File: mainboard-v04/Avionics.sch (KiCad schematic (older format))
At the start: 36 parts, among them J10 Conn_01x05, J8 Conn_01x09, J9 Conn_01x05, SW1 KMR231NG LFS, U1 MAX706RS-T, U2 ATSAMD51J20A-AU, U3 BMX160, Y1 32.768kHz

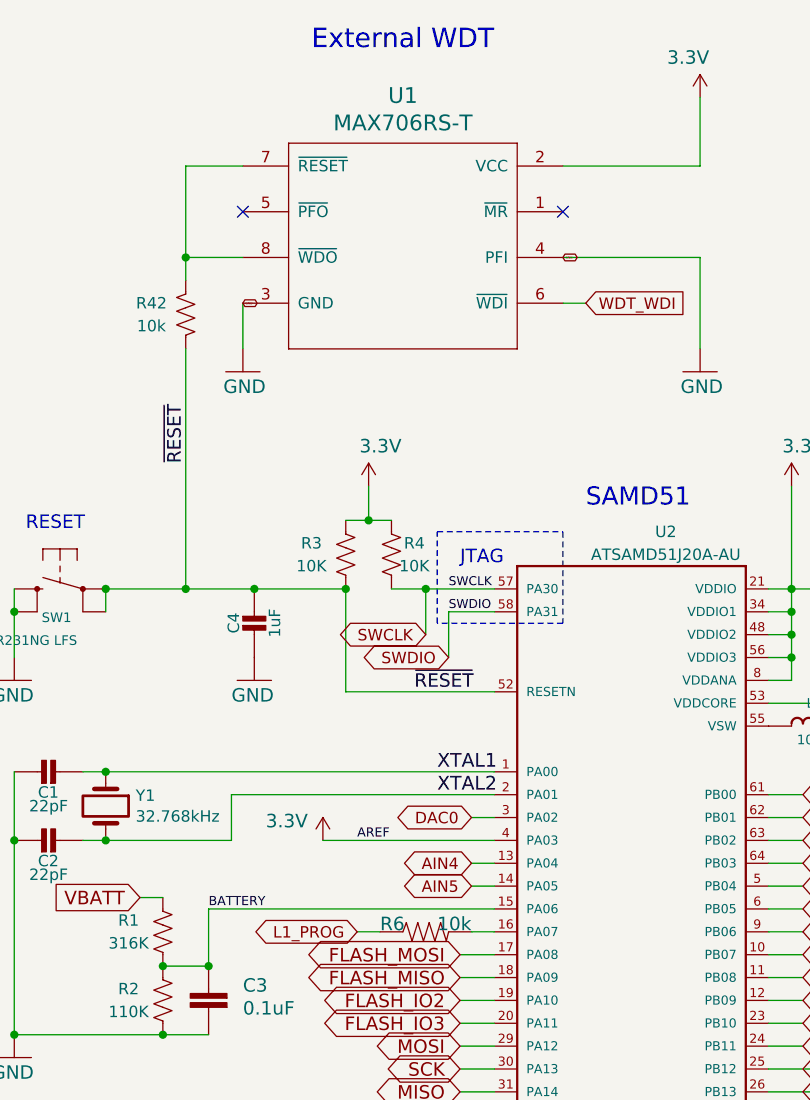
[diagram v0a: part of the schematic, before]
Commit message: adding mainbaordv04 layout and BOM
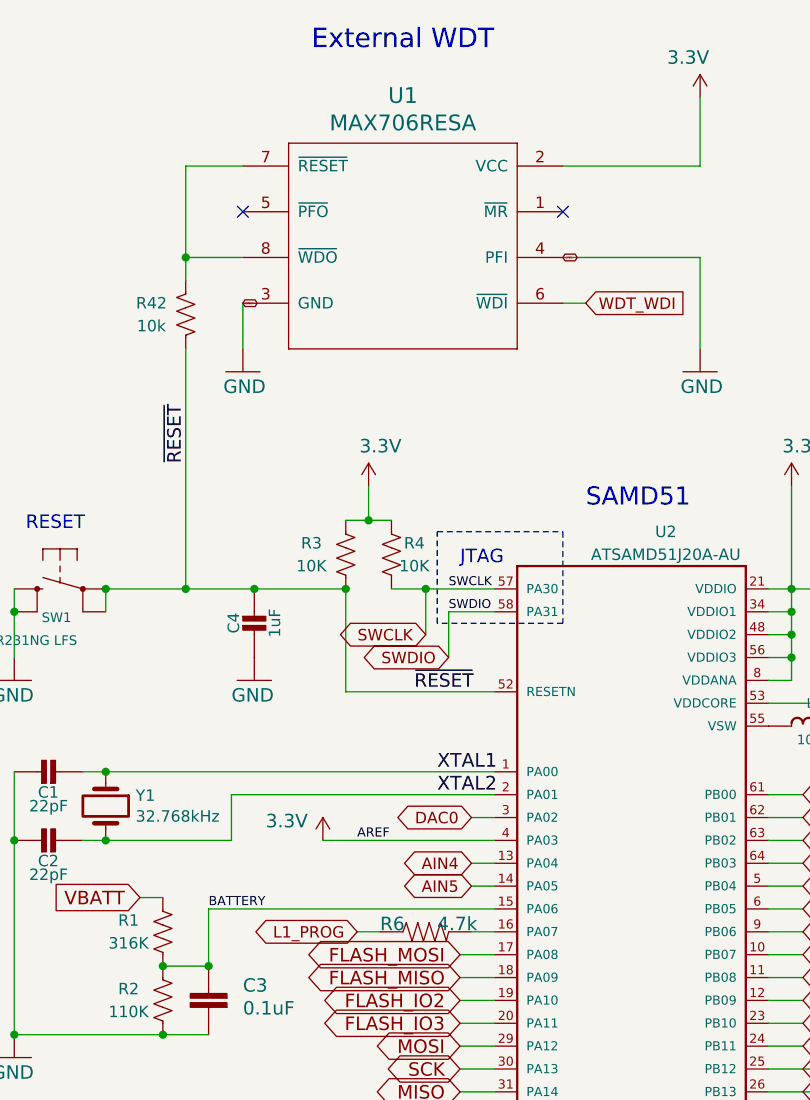
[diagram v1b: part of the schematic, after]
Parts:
- D1: Flight (none) -> WS2812B; Proto (none) -> WS2812B
- L1: footprint Inductor_SMD:L_0806_2016Metric -> Inductor_SMD:L_0805_2012Metric_Pad1.15x1.40mm_HandSolder
- R6: value 10k -> 4.7k
- U1: value MAX706RS-T -> MAX706RESA; Flight (none) -> MAX706RESA; Proto (none) -> MAX706RESA
- U2: Field8 Unavailable -> (none); Flight (none) -> ATSAMD51J20A-AU; Proto (none) -> ATSAMD51J20A-AU
- U3: Flight (none) -> BMX160; Height 1 -> (none); Manufacturer_Name Bosch -> (none); Manufacturer_Part_Number BMX160 -> (none); Mouser Part Number 262-BMX160 -> (none); Proto (none) -> BMX160
- Y1: Flight (none) -> ABS07-32.768KHZ-T; Proto (none) -> ABS07-32.768KHZ-T
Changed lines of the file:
@@
 EESchema Schematic File Version 4
-LIBS:mainboard-cache
 EELAYER 30 0
 EELAYER END
@@
 Sheet 6 6
 Title "PyCubed Mainboard"
-Date "2019-11-27"
+Date "2020-01-08"
 Rev "v04"
-Comp "Stanford University"
+Comp ""
 Comment1 "Zac Manchester"
 Comment2 "Max Holliday"
@@
 AR Path="/5CEC5A72/B13F4994" Ref="R6"  Part="1"
 F 0 "R6" H 4200 4650 59  0000 L BNN
-F 1 "10k" H 4450 4650 59  0000 L BNN
+F 1 "4.7k" H 4450 4650 59  0000 L BNN
 F 2 "Resistor_SMD:R_0603_1608Metric" H 4400 4650 50  0001 C CNN
 F 3 "" H 4400 4650 50  0001 C CNN
@@
 F 0 "L1" H 6100 3850 42  0000 C CNN
 F 1 "10uH" H 6100 3690 42  0000 C CNN
-F 2 "Inductor_SMD:L_0806_2016Metric" H 6100 3750 50  0001 C CNN
+F 2 "Inductor_SMD:L_0805_2012Metric_Pad1.15x1.40mm_HandSolder" H 6100 3750 50  0001 C CNN
 F 3 "https://product.tdk.com/info/en/catalog/datasheets/inductor_commercial_power_vls201610hbx-1_en.pdf" H 6100 3750 50  0001 C CNN
 	1    6100 3750
@@
 F 2 "Crystal:Crystal_SMD_3215-2Pin_3.2x1.5mm" H 3000 4100 50  0001 C CNN
 F 3 "~" H 3000 4100 50  0001 C CNN
+F 4 "ABS07-32.768KHZ-T" H 3000 4100 50  0001 C CNN "Flight"
+F 5 "ABS07-32.768KHZ-T" H 3000 4100 50  0001 C CNN "Proto"
 	1    3000 4100
 	0    1    1    0
@@
 P 5100 1400
 F 0 "U1" H 5900 1808 69  0000 C CNN
-F 1 "MAX706RS-T" H 5900 1688 69  0000 C CNN
+F 1 "MAX706RESA" H 5900 1688 69  0000 C CNN
 F 2 "Package_SO:SO-8_3.9x4.9mm_P1.27mm" H 5100 1400 50  0001 C CNN
 F 3 "" H 5100 1400 50  0001 C CNN
+F 4 "MAX706RESA" H 5100 1400 50  0001 C CNN "Flight"
+F 5 "MAX706RESA" H 5100 1400 50  0001 C CNN "Proto"
 	1    5100 1400
 	-1   0    0    -1
@@
 F 6 "None" H 5300 4950 50  0001 L BNN "Field6"
 F 7 "ATSAMD51J20A-AU" H 5300 4950 50  0001 L BNN "Field7"
-F 8 "Unavailable" H 5300 4950 50  0001 L BNN "Field8"
+F 8 "" H 5300 4950 50  0001 L BNN "Field8"
+F 9 "ATSAMD51J20A-AU" H 5300 4950 50  0001 C CNN "Flight"
+F 10 "ATSAMD51J20A-AU" H 5300 4950 50  0001 C CNN "Proto"
 	1    5300 4950
 	1    0    0    -1
@@
 F 2 "LED_SMD:LED_WS2812B_PLCC4_5.0x5.0mm_P3.2mm" H 3150 5750 50  0001 L TNN
 F 3 "https://cdn-shop.adafruit.com/datasheets/WS2812B.pdf" H 3200 5675 50  0001 L TNN
+F 4 "WS2812B" H 3100 6050 50  0001 C CNN "Flight"
+F 5 "WS2812B" H 3100 6050 50  0001 C CNN "Proto"
 	1    3100 6050
 	-1   0    0    -1
@@
 F 3 "https://ae-bst.resource.bosch.com/media/_tech/media/datasheets/BST-BMX160-DS000.pdf" H 10250 4850 50  0001 L CNN
 F 4 "IMUs - Inertial Measurement Units 9-axis (9DOF) Absolute Orientation MEMS Sensor" H 10250 4750 50  0001 L CNN "Description"
-F 5 "1" H 10250 4650 50  0001 L CNN "Height"
-F 6 "Bosch" H 10250 4550 50  0001 L CNN "Manufacturer_Name"
-F 7 "BMX160" H 10250 4450 50  0001 L CNN "Manufacturer_Part_Number"
-F 8 "262-BMX160" H 10250 4350 50  0001 L CNN "Mouser Part Number"
+F 5 "" H 10250 4650 50  0001 L CNN "Height"
+F 6 "" H 10250 4550 50  0001 L CNN "Manufacturer_Name"
+F 7 "" H 10250 4450 50  0001 L CNN "Manufacturer_Part_Number"
+F 8 "" H 10250 4350 50  0001 L CNN "Mouser Part Number"
+F 9 "BMX160" H 9200 4850 50  0001 C CNN "Flight"
+F 10 "BMX160" H 9200 4850 50  0001 C CNN "Proto"
 	1    9200 4850
 	-1   0    0    -1

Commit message: cleaned up v04
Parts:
- added C5: 0.1uF, Capacitor_SMD:C_0603_1608Metric, symbol mainboard:0.1UF-25V(+80_-20%)(0603)
- added R41: 10k, Resistor_SMD:R_0603_1608Metric, symbol mainboard:R-US_R0603
- J10, J8, J9, R42: DNI (none) -> DNI
- U2: value ATSAMD51J20A-AU -> 120MHZ 512KB Flash 64 TQFP; Field4 120MHZ 1024KB Flash 64 TQFP PKG inTray 85CTemp, 64 TQFP 10x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 -> 120MHZ 512KB Flash 64 TQFP PKG inTray 85CTemp, 64 TQFP 10x1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; Field6 None -> (none); Field7 ATSAMD51J20A-AU -> (none); Flight ATSAMD51J20A-AU -> ATSAMD51J19A-AU; Proto ATSAMD51J20A-AU -> ATSAMD51J19A-AU
- U3: footprint BMX160 -> custom-footprints:BMX160
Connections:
- net at D1.1 (VDD): now also C5.1
- net at D1.3 (VSS): now also C5.2
- net at U3.1 (SDO): now also R41.1
- net at U3.2 (GND_1), U3.3 (GND_2): now also R41.2
- net xSDCS renamed SD_CS
- no-connect marks 8 -> 7
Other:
- note added: "0x68"
- note added: "I2C ADDR"
- note added: "IMU"
- note added: "NOTE: Components labeled "do not install" (DNI) are not populated by default"
- note added: "TCK\nTMS"
- note added: "WDT enabled\nwhen installed"
- note removed: "IMU - BMX160"
- moved on the sheet: C1, C10, C11, C12, C13, C14, C15, C16, C2, C3, C4, C7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
